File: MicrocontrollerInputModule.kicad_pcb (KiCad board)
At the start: 2 copper layers, 31 x 111.4 mm, 370 parts, among them J2 FH34SRJ-12S-0.5SH_50_, SW1 KXT3, SW2 KXT3, U1 W25Q16JVUXIQ, U2 RP2040, U3 74AHC125BQ_115, U4 74AHC125BQ_115, Y1 12.000MHz

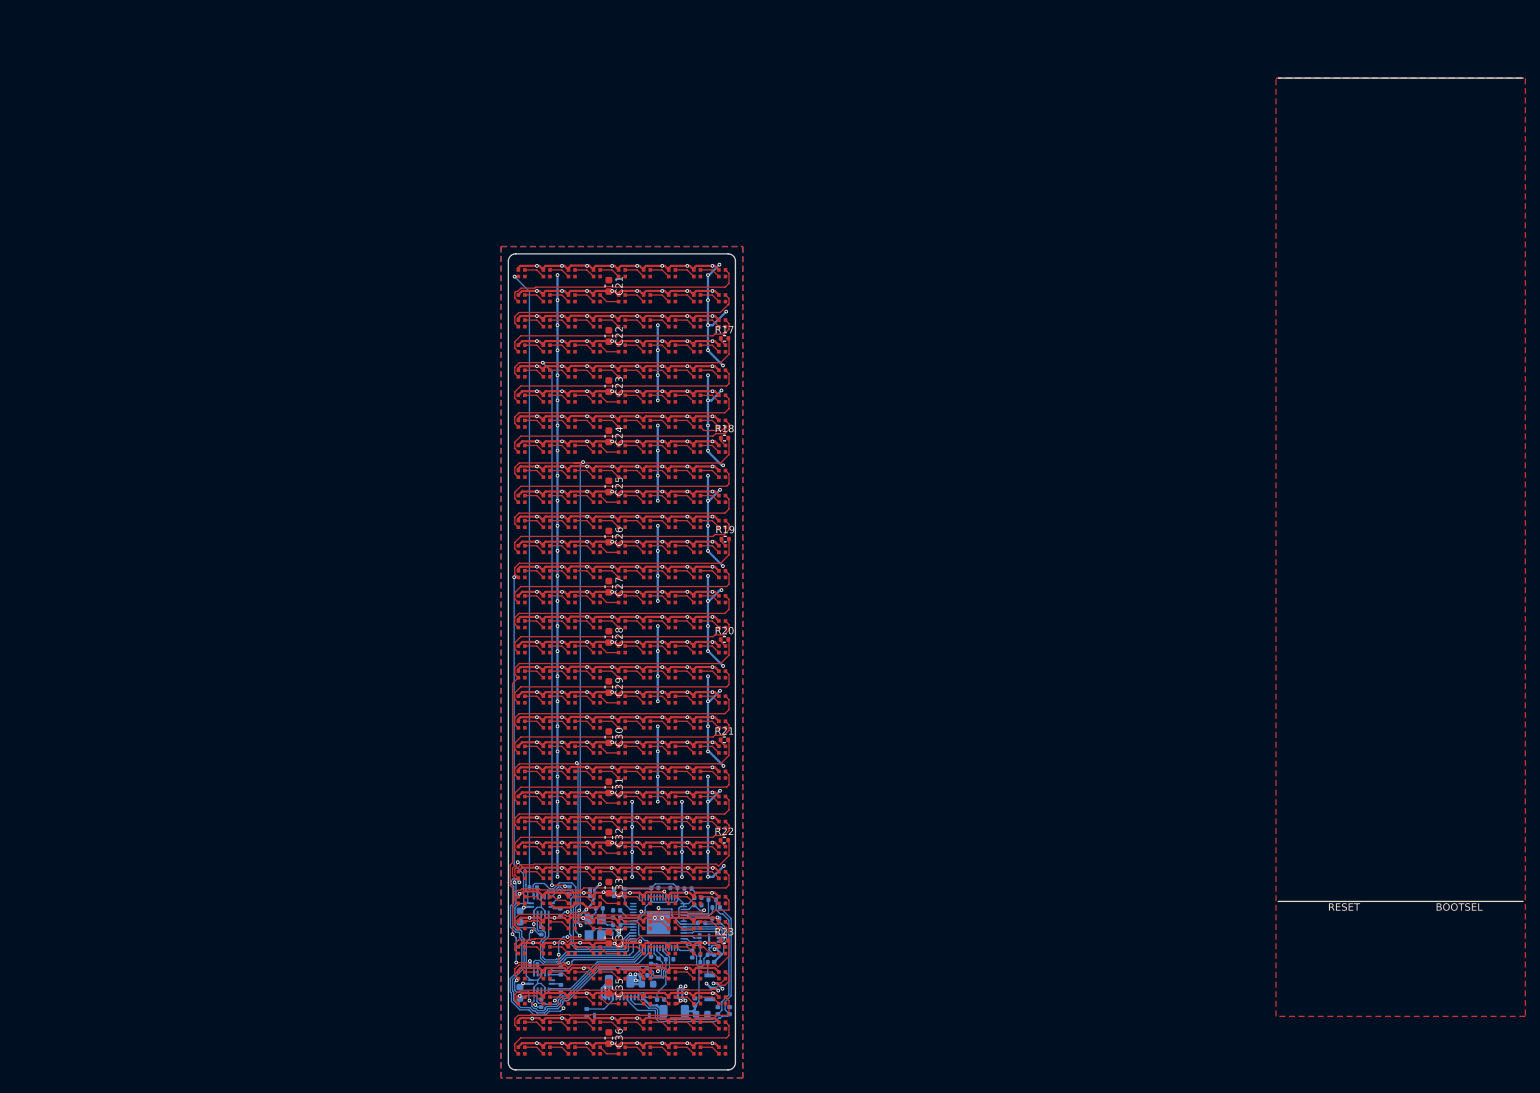
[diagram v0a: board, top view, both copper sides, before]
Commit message: Added silkscreen
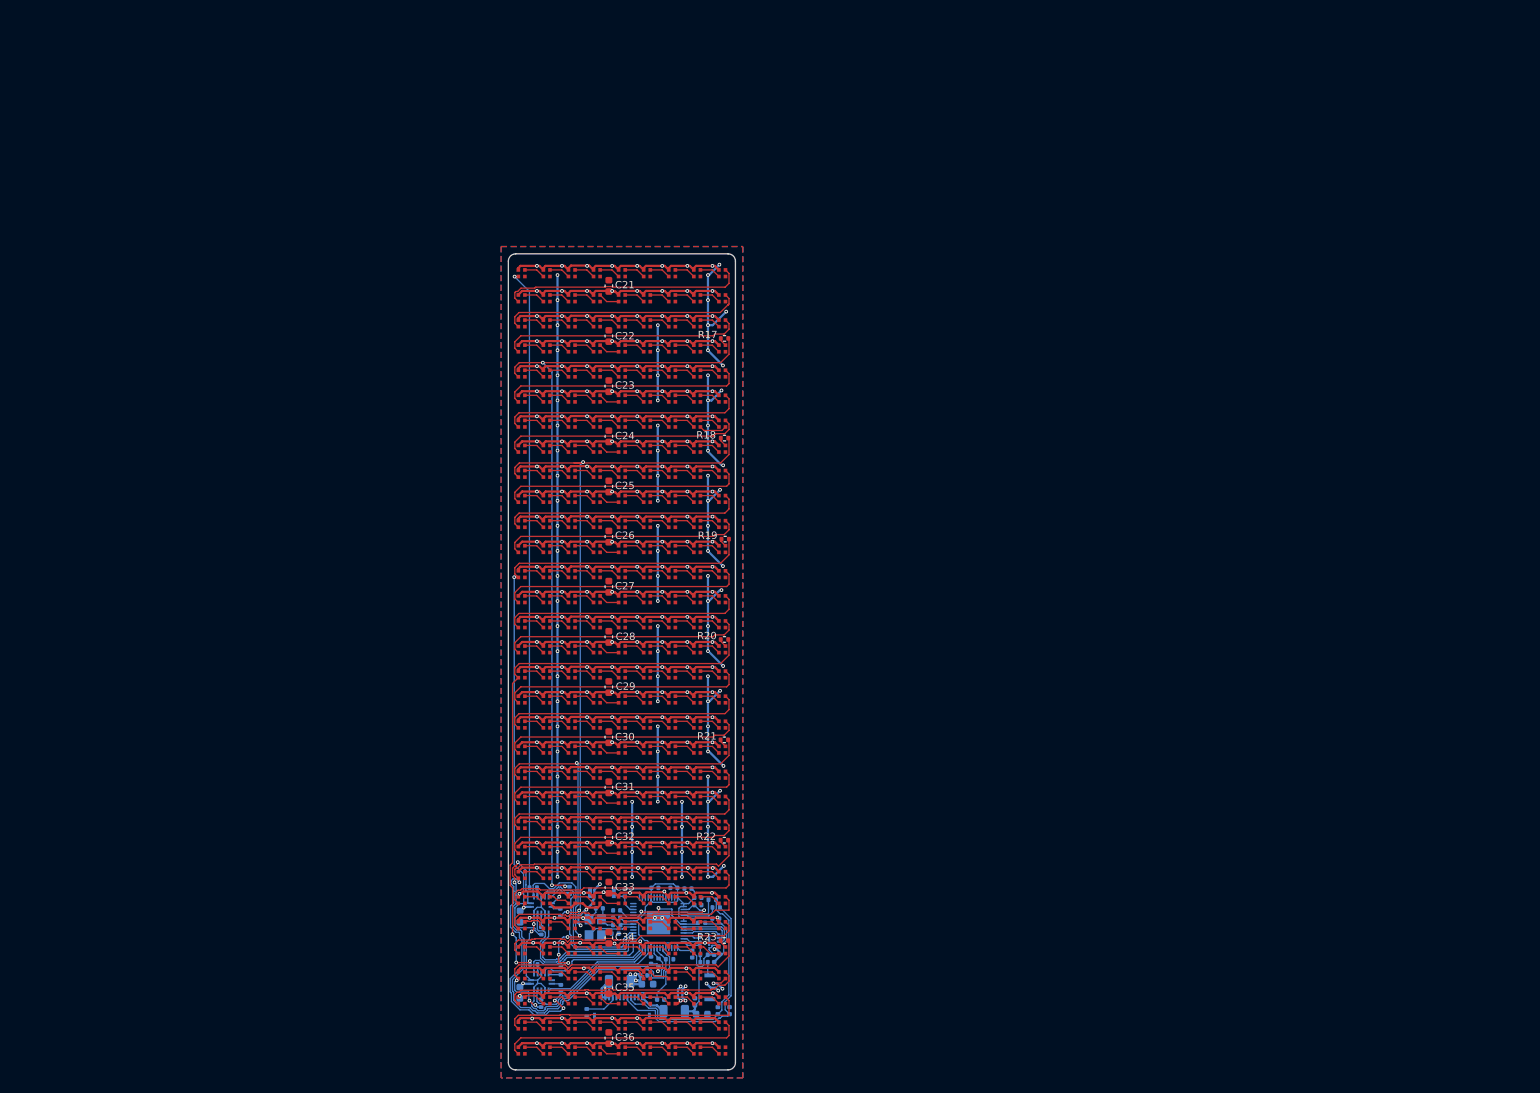
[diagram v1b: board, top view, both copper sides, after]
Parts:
- moved G*** 117.3 mm to (90.1, 129.7)
- moved G*** 112.5 mm to (103.2, 97.3)
- moved G*** 106.7 mm to (103.2, 159.1)
- moved G*** 102.7 mm to (101.4, 129.4)
- moved G*** 102.4 mm to (98.7, 129.4)
- moved G*** 102.2 mm to (95.9, 129.4)
- moved G*** 102.0 mm to (93.1, 129.4)
- moved G*** 74.6 mm to (103.2, 60.3)
- moved G*** 74.2 mm to (103.2, 76.3)
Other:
- board text added: "BOOT"
- board text added: "LED Strip | GPIO Pin 1 Top | D15 2 | D14 3 | D13 4 | D12 5 | D11 6 | D10 7 | D9 8 Bot | D8"
- board text added: "Set GPIO pin D7 high to disable all level shifter outputs except Strip 1 D15"
- board text added: "TOP: Strip 1 is on the other side of this text"
- board text added: "by Joe Schroedl, v2"
- board text removed: "BOOTSEL"
- board text removed: "LED Strip | GPIO Pin 1 | D23 2 | D22 3 | D21 4 | D17 5 | D16 6 | D15 7 | D14 8 | D13"
- board text removed: "LED Strip | GPIO Pin 9 | D12 10 | D11 11 | D10 12 | D9 13 | D8 14 | D7 15 | D6 16 | D5"
- board text removed: "by Joe Schroedl, v1"

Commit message: PCB Assembly and Production Files
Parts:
- moved N139 65.3 mm to (42.7, 72.0)
- moved N148 65.3 mm to (42.7, 75.5)
- moved N274 65.3 mm to (42.7, 123.4)
- moved N283 65.3 mm to (42.7, 126.8)
- moved R6 65.3 mm to (58.4, 106.2)
- moved U1 65.3 mm to (58.0, 111.7)
- moved C1 65.3 mm to (45.2, 110.9)
- moved C12 65.3 mm to (50.1, 114.5)
- moved C18 65.3 mm to (32.2, 118.9)
- moved C6 65.3 mm to (56.5, 107.0)
- moved C7 65.3 mm to (55.1, 104.7)
- moved C8 65.3 mm to (56.5, 105.9)
- moved G*** 65.3 mm to (44.3, 97.7)
- moved G*** 65.3 mm to (41.6, 97.8)
- moved G*** 65.3 mm to (38.8, 97.8)
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
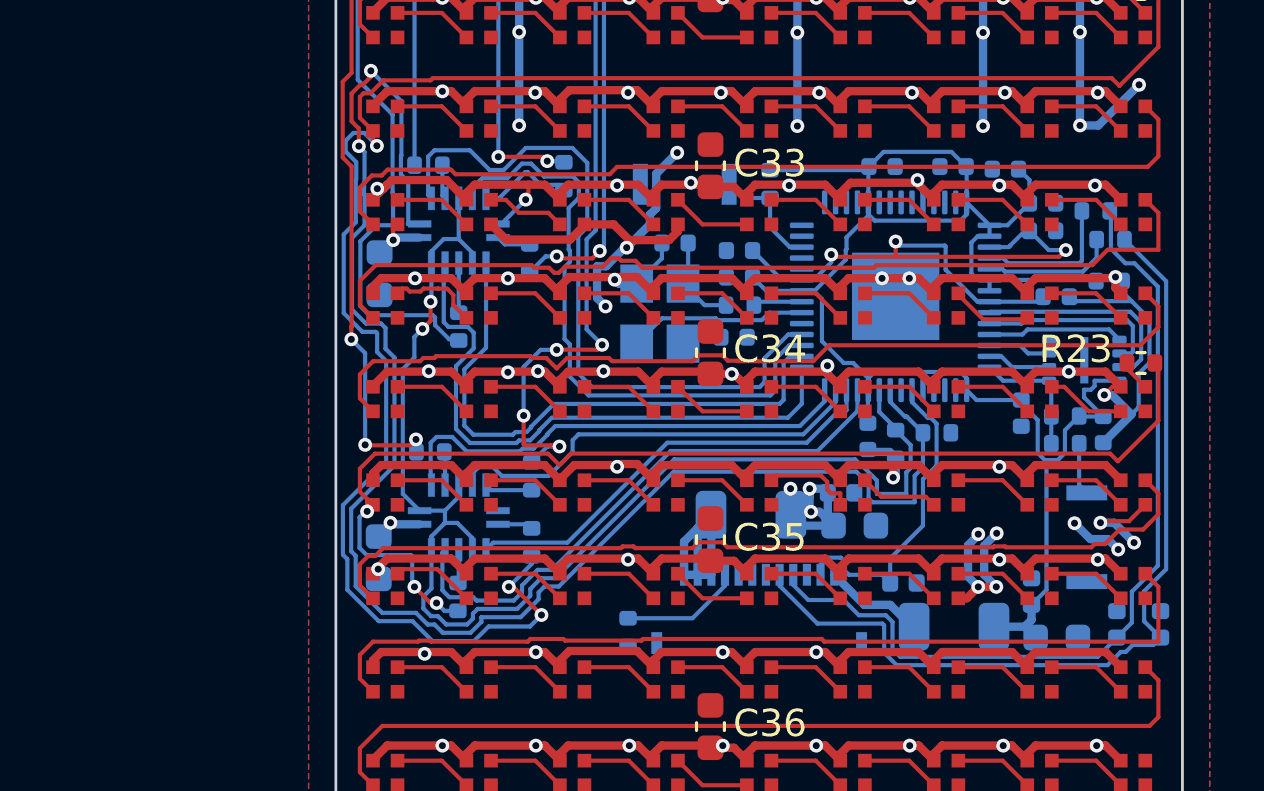
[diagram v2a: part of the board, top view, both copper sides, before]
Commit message: Added dip switch
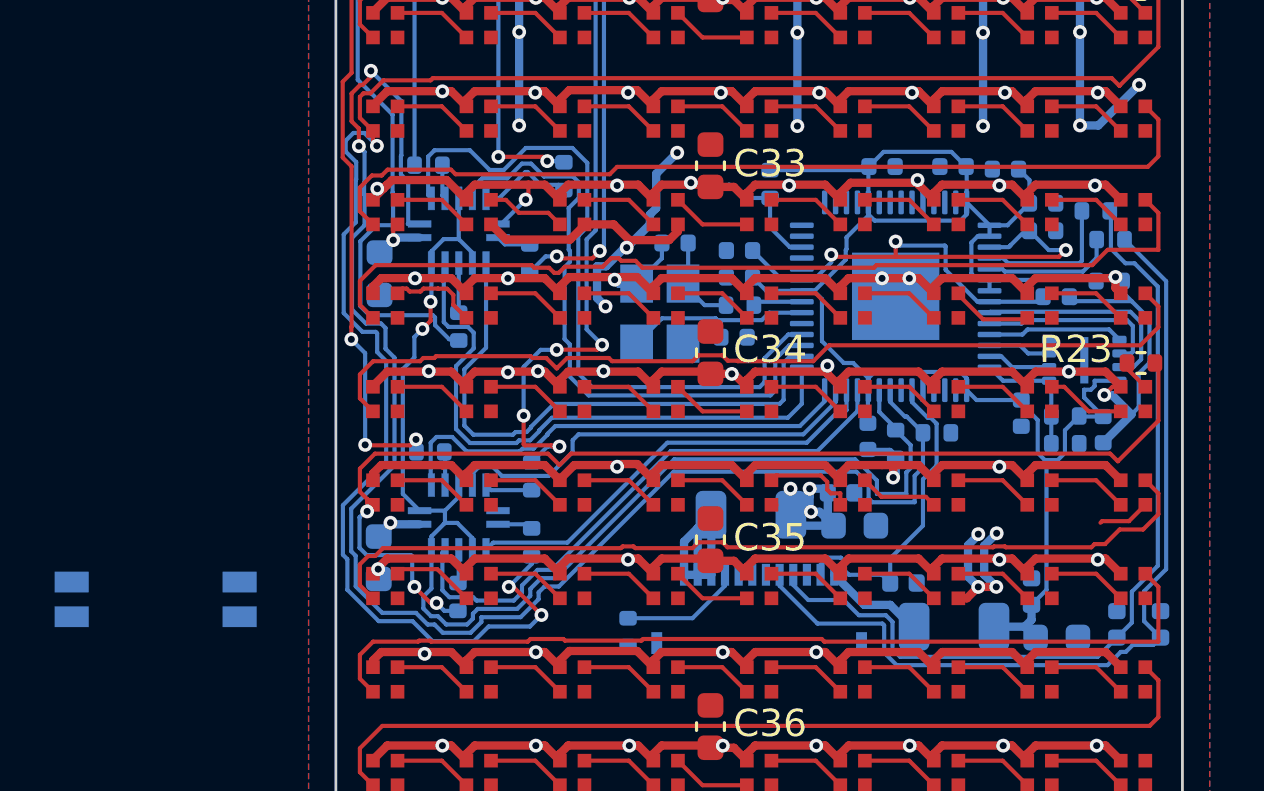
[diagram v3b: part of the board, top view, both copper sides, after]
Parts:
- removed SW1, SW2: KXT3, Button_Switch_SMD:SW_SPST_CK_KXT3
- added SW3: A6H-2101, footprints:SW_A6H-2101_OMR, B.Cu at (24.0, 120.5)
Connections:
- net /~{RESET} renamed ~{RESET}
- R1 pad 1: Net-(R1-Pad1) -> BOOTSEL
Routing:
- net +5V: track 297.3 -> 293.8 mm, vias 107 -> 103
- net Net-(R1-Pad1): track 1.92 -> 0.00 mm
